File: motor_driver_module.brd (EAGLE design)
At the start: 160 x 100 mm, 48 parts, among them IC3 LTC6087, IC4 LTC6087, IC7 DRV8833RTY, IC8 DRV8833RTY, P1 BAT+, P10 MD2, P11 MA_IN1, P12 MA_IN2, P13 MB_IN1, P14 MB_IN2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

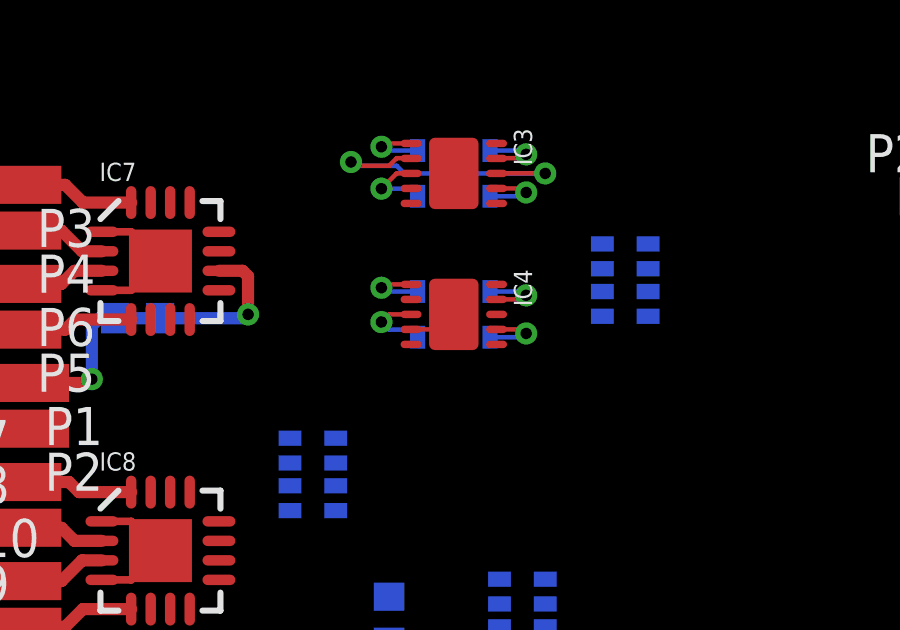
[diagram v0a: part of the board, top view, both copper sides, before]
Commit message: Further routing for super space efficiency.
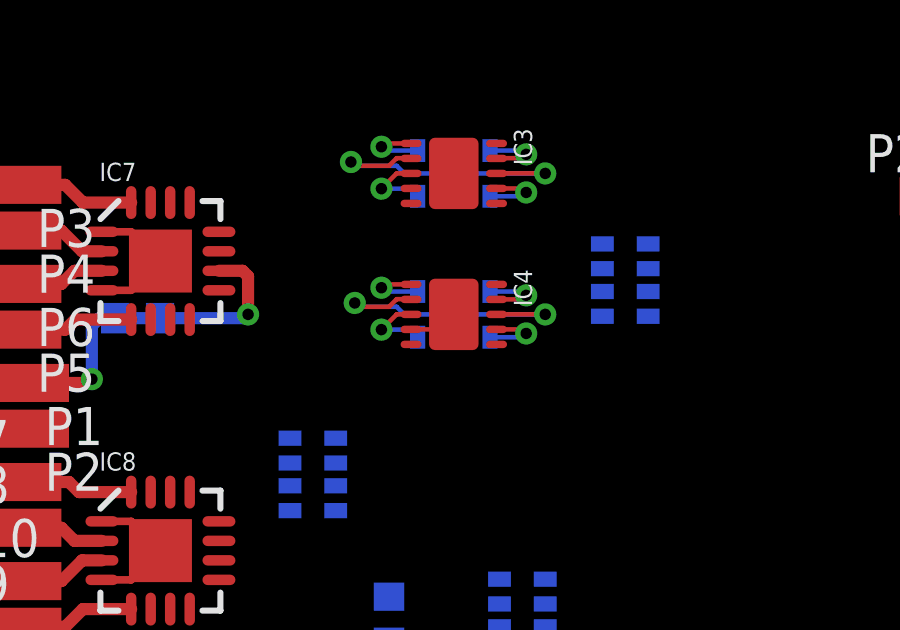
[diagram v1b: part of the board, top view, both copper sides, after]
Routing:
- net N$25: track 0.00 -> 5.80 mm, vias 0 -> 1
- net N$27: track 0.00 -> 4.98 mm, vias 0 -> 1
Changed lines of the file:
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@@
 <contactref element="R33" pad="6"/>
 <contactref element="R8" pad="7"/>
-<wire x1="10.16" y1="8.763" x2="17.046" y2="19.177" width="0" layer="19" extent="1-16"/>
 <wire x1="16.002" y1="19.939" x2="16.002" y2="19.304" width="0.1524" layer="16"/>
 <wire x1="16.002" y1="19.304" x2="16.129" y2="19.177" width="0.1524" layer="16"/>
@@
 <via x="18.669" y="19.177" extent="1-16" drill="0.381"/>
 <wire x1="18.669" y1="19.177" x2="17.046" y2="19.177" width="0.1524" layer="1"/>
+<wire x1="10.16" y1="8.763" x2="16.129" y2="19.177" width="0" layer="19" extent="16-16"/>
 </signal>
 <signal name="N$24">
@@
 <contactref element="IC4" pad="3"/>
 <contactref element="R1" pad="4"/>
-<wire x1="14.196" y1="14.478" x2="13.462" y2="14.478" width="0.1524" layer="1"/>
-<wire x1="13.462" y1="14.478" x2="13.208" y2="14.224" width="0.1524" layer="1"/>
-<via x="13.208" y="14.224" extent="1-16" drill="0.381"/>
-<wire x1="13.208" y1="14.224" x2="13.462" y2="13.97" width="0.1524" layer="16"/>
-<wire x1="13.462" y1="13.97" x2="14.1605" y2="13.97" width="0.1524" layer="16"/>
+<wire x1="14.196" y1="14.478" x2="13.716" y2="14.478" width="0.1524" layer="1"/>
+<wire x1="13.716" y1="14.478" x2="13.208" y2="13.97" width="0.1524" layer="1"/>
+<via x="13.208" y="13.97" extent="1-16" drill="0.381"/>
+<wire x1="13.208" y1="13.97" x2="14.1605" y2="13.97" width="0.1524" layer="16"/>
 <wire x1="14.1605" y1="13.97" x2="14.4145" y2="13.716" width="0.1524" layer="16"/>
 <wire x1="14.4145" y1="13.716" x2="22.098" y2="14.4145" width="0" layer="19" extent="16-16"/>
@@
 <contactref element="IC4" pad="2"/>
 <contactref element="R1" pad="6"/>
+<wire x1="15.24" y1="15.24" x2="15.24" y2="14.605" width="0.1524" layer="16"/>
+<wire x1="15.24" y1="14.605" x2="15.113" y2="14.478" width="0.1524" layer="16"/>
+<wire x1="15.113" y1="14.478" x2="13.97" y2="14.478" width="0.1524" layer="16"/>
+<wire x1="13.97" y1="14.478" x2="13.716" y2="14.732" width="0.1524" layer="16"/>
+<wire x1="13.716" y1="14.732" x2="12.446" y2="14.732" width="0.1524" layer="16"/>
+<wire x1="12.446" y1="14.732" x2="12.319" y2="14.859" width="0.1524" layer="16"/>
+<via x="12.319" y="14.859" extent="1-16" drill="0.381"/>
+<wire x1="12.319" y1="14.859" x2="12.446" y2="14.732" width="0.1524" layer="1"/>
+<wire x1="12.446" y1="14.732" x2="13.462" y2="14.732" width="0.1524" layer="1"/>
+<wire x1="13.462" y1="14.732" x2="13.716" y2="14.986" width="0.1524" layer="1"/>
+<wire x1="13.716" y1="14.986" x2="14.188" y2="14.986" width="0.1524" layer="1"/>
+<wire x1="14.188" y1="14.986" x2="14.196" y2="14.978" width="0.1524" layer="1"/>
 <wire x1="15.24" y1="15.24" x2="22.098" y2="15.24" width="0" layer="19" extent="16-16"/>
-<wire x1="14.196" y1="14.978" x2="15.24" y2="15.24" width="0" layer="19" extent="1-16"/>
 </signal>
 <signal name="N$26">
@@
 <contactref element="IC4" pad="8"/>
 <contactref element="R1" pad="7"/>
-<wire x1="17.046" y1="14.478" x2="22.098" y2="16.8275" width="0" layer="19" extent="1-16"/>
-<wire x1="16.002" y1="15.24" x2="17.046" y2="14.478" width="0" layer="19" extent="1-16"/>
+<wire x1="16.002" y1="15.24" x2="16.002" y2="14.605" width="0.1524" layer="16"/>
+<wire x1="16.002" y1="14.605" x2="16.129" y2="14.478" width="0.1524" layer="16"/>
+<wire x1="16.129" y1="14.478" x2="18.669" y2="14.478" width="0.1524" layer="16"/>
+<via x="18.669" y="14.478" extent="1-16" drill="0.381"/>
+<wire x1="18.669" y1="14.478" x2="17.046" y2="14.478" width="0.1524" layer="1"/>
+<wire x1="18.669" y1="14.478" x2="22.098" y2="16.8275" width="0" layer="19" extent="16-16"/>
 </signal>
 <signal name="MOTOR_D_BEMF">

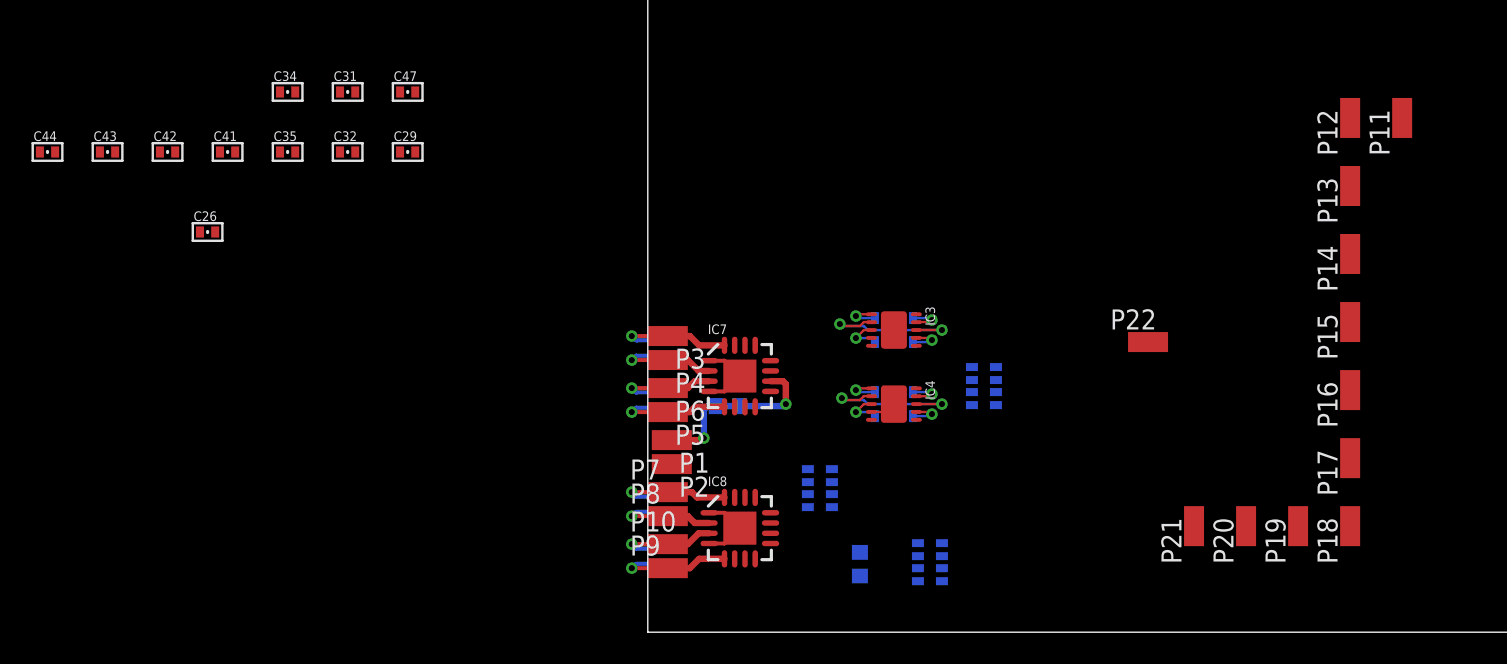
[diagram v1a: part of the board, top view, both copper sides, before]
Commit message: More rerouting. Minimal size does not look promising as of right now.
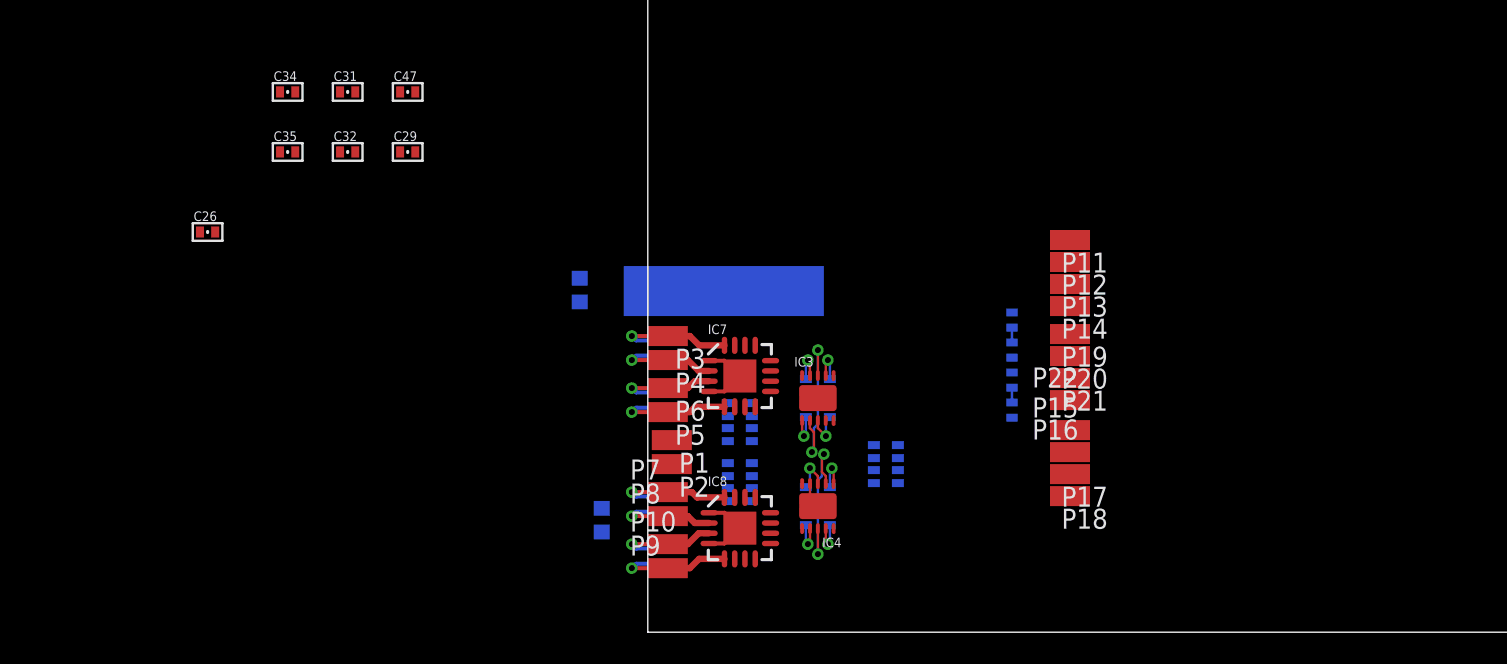
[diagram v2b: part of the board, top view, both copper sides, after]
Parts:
- moved C44 63.4 mm to (23.1, 14.1), flipped to the bottom, turned to 90 degrees
- moved C43 59.2 mm to (23.1, 16.0), flipped to the bottom, turned to 270 degrees
- moved C42 55.0 mm to (23.1, 17.9), flipped to the bottom, turned to 90 degrees
- moved C41 50.9 mm to (23.1, 19.8), flipped to the bottom, turned to 270 degrees
- moved P11 22.5 mm to (26.8, 24.9), turned to 90 degrees
- moved P12 20.0 mm to (26.8, 23.5), turned to 90 degrees
- moved P15 19.1 mm to (26.8, 12.8), turned to 270 degrees
- moved P19 18.9 mm to (26.8, 18.9), turned to 90 degrees
- moved P13 18.8 mm to (26.8, 22.1), turned to 90 degrees
- moved P16 18.2 mm to (26.8, 11.4), turned to 270 degrees
- moved P14 18.1 mm to (26.8, 20.7), turned to 90 degrees
- moved P18 17.9 mm to (26.8, 8.64), turned to 90 degrees
- moved P17 17.8 mm to (26.8, 10.0), turned to 90 degrees
- moved R34 16.7 mm to (5.84, 9.53)
- moved C30 16.6 mm to (-2.92, 7.11)
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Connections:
- net MOTOR_A_BEMF: now also R3.1; no longer R3.8
- net MOTOR_A_OUT1: now also R33.7; no longer R33.1
- net MOTOR_A_OUT2: now also R33.8; no longer R33.2
- net MOTOR_B_BEMF: now also R3.2; no longer R3.7
- net MOTOR_C_BEMF: now also R3.3; no longer R3.6
- net MOTOR_D_BEMF: now also R3.4; no longer R3.5
- net N$30: now also R33.2; no longer R33.8
- net N$31: now also R33.1; no longer R33.7
- net N$34: now also R3.5; no longer R3.4
- net N$35: now also R3.6; no longer R3.3
- net N$36: now also R3.8; no longer R3.1
- net N$37: now also R3.7; no longer R3.2
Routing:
- net V_BATT: track 11.5 -> 0.00 mm, vias 2 -> 0
- net GND: track 11.0 -> 12.9 mm

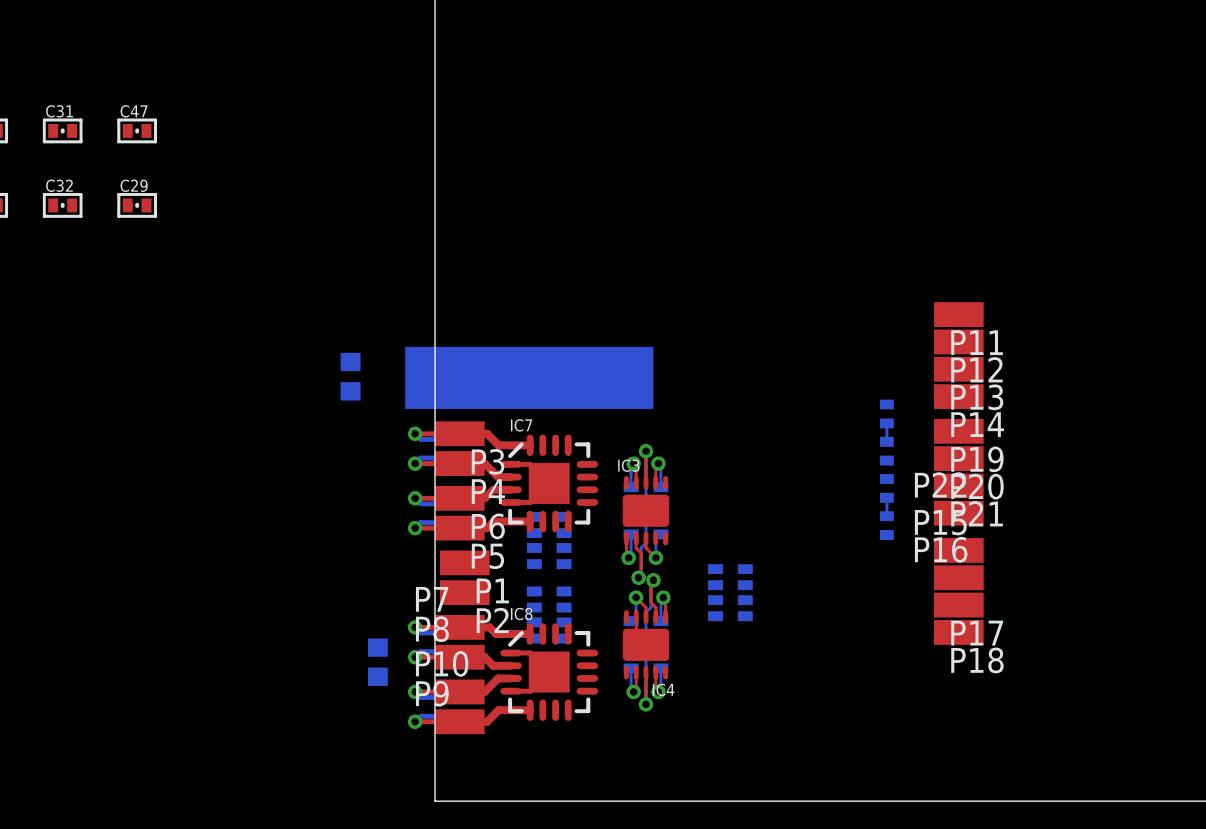
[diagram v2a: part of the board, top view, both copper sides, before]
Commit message: Appears more promising to use LTC6088 and discrete resistors.
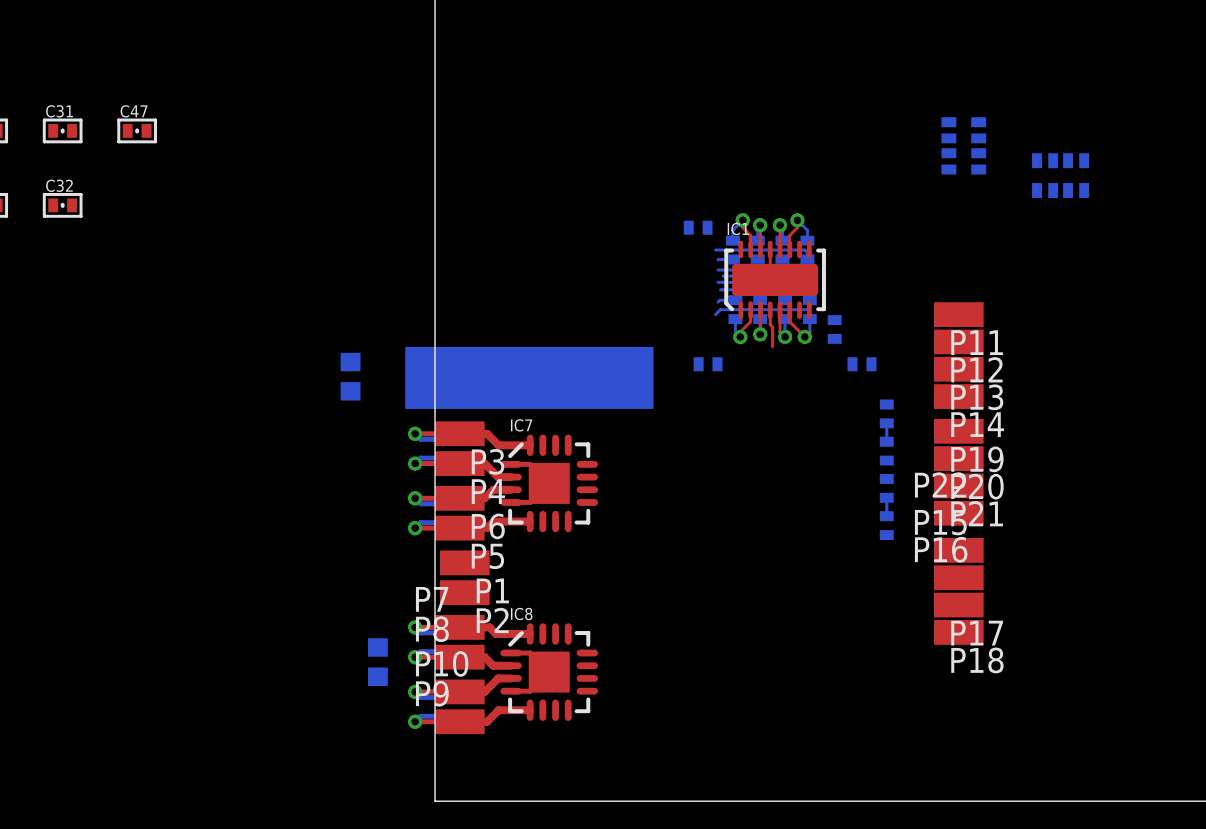
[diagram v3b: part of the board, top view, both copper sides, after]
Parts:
- removed C29: 0.1uF, biomimetic:0402-CAP
- removed IC3, IC4: LTC6087, biomimetic:DFN-10
- removed R33, R34: 47k, OPL Eagle Library:R1206-8
- added IC1: LTC6088, biomimetic:DFN-16
- added R10, R11, R12, R13, R14, R2, R4, R5, R6, R7, R9: (no value), biomimetic:0402-RES
- R3: value 1K -> (none); device OPL Eagle Library:R1206-8 -> biomimetic:0402-RES
- moved R1 32.0 mm to (32.0, 32.0), turned to 180 degrees
- moved R8 24.8 mm to (27.1, 33.5)
- moved R3 11.7 mm to (14.0, 22.4), turned to 0 degrees
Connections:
- net 3.3V: now also IC1.4; no longer C29.1, IC3.10, IC4.10
- net GND: now also IC1.13, IC1.PAD; no longer C29.2, IC3.4, IC3.PAD, IC4.4, IC4.PAD
- net MOTOR_A_BEMF: now also R3.2; no longer R3.1
- net MOTOR_A_OUT1: now also R2.1; no longer R33.7
- net MOTOR_A_OUT2: now also R4.1; no longer R33.8
- net MOTOR_B_BEMF: now also R12.2; no longer R3.2
- net MOTOR_B_OUT1: now also R5.1; no longer R33.4
- net MOTOR_B_OUT2: now also R6.1; no longer R33.3
- net MOTOR_C_BEMF: now also R13.2; no longer R3.3
- net MOTOR_C_OUT1: now also R7.1; no longer R34.1
- net MOTOR_C_OUT2: now also R9.1; no longer R34.2
- net MOTOR_D_BEMF: now also R14.2; no longer R3.4
- net MOTOR_D_OUT1: now also R10.1; no longer R34.3
- net MOTOR_D_OUT2: now also R11.1; no longer R34.4
- net N$22: now also IC1.14, R5.2; no longer IC3.7, R33.5
- net N$23: now also IC1.15, R6.2; no longer IC3.8, R33.6
- net N$24: now also IC1.5, R7.2; no longer IC4.3, R34.8
- net N$25: now also IC1.6, R9.2; no longer IC4.2, R34.7
- net N$26: now also IC1.12, R10.2; no longer IC4.7, R34.6
- net N$27: now also IC1.11, R11.2; no longer IC4.8, R34.5
- net N$30: now also IC1.3, R2.2; no longer IC3.3, R33.2
- net N$31: now also IC1.2, R4.2; no longer IC3.2, R33.1
- net N$34: now also IC1.10, R14.1; no longer IC4.9, R3.5
- net N$35: now also IC1.7, R13.1; no longer IC4.1, R3.6
- net N$36: now also IC1.1, R3.1; no longer IC3.1, R3.8
- net N$37: now also IC1.16, R12.1; no longer IC3.9, R3.7
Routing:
- net MOTOR_C_OUT2: track 6.60 -> 11.9 mm
- net MOTOR_D_OUT2: track 6.96 -> 12.1 mm
- net MOTOR_C_OUT1: track 7.53 -> 11.6 mm
- net MOTOR_D_OUT1: track 7.89 -> 11.5 mm
- net N$31: track 6.06 -> 2.61 mm
- net N$25: track 5.80 -> 2.71 mm
- net MOTOR_B_OUT1: track 7.79 -> 10.3 mm
- net MOTOR_A_OUT1: track 7.89 -> 10.4 mm
- net N$34: track 2.30 -> 0.00 mm, vias 1 -> 0
- net N$37: track 2.30 -> 0.00 mm, vias 1 -> 0
- net N$35: track 2.29 -> 0.00 mm, vias 1 -> 0
- net N$36: track 2.29 -> 0.00 mm, vias 1 -> 0
- net N$23: track 4.98 -> 2.91 mm
- net N$27: track 4.98 -> 2.91 mm
- net 3.3V: track 0.00 -> 1.93 mm
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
